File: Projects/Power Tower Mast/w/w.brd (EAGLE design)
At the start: 15 x 20.9 mm, 25 parts

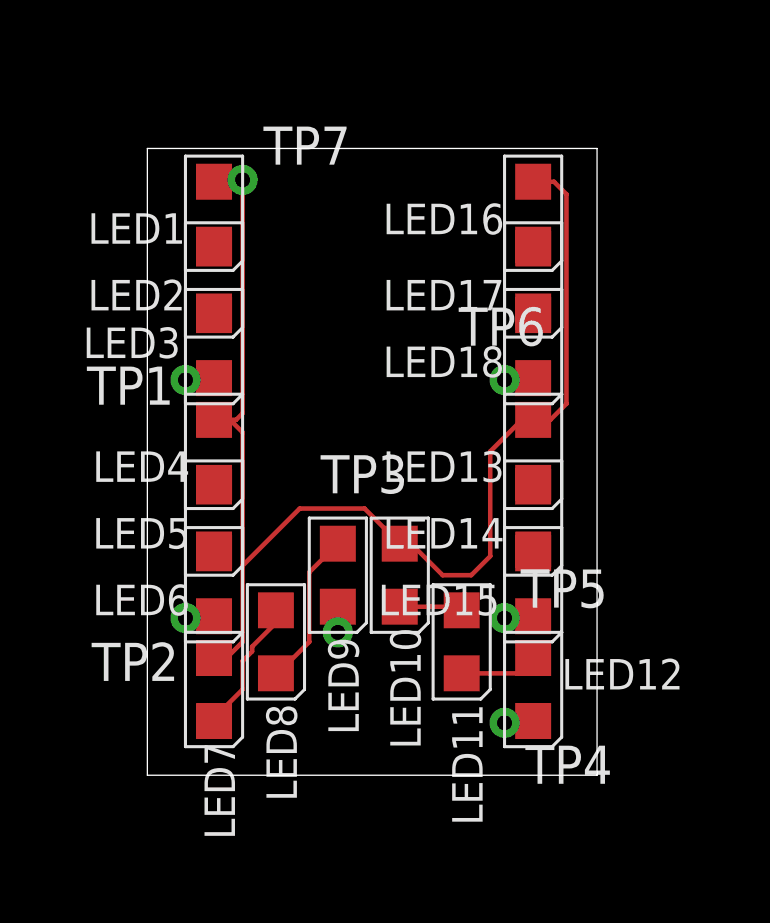
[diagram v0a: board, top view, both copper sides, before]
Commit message: updated with extra vias and panelized
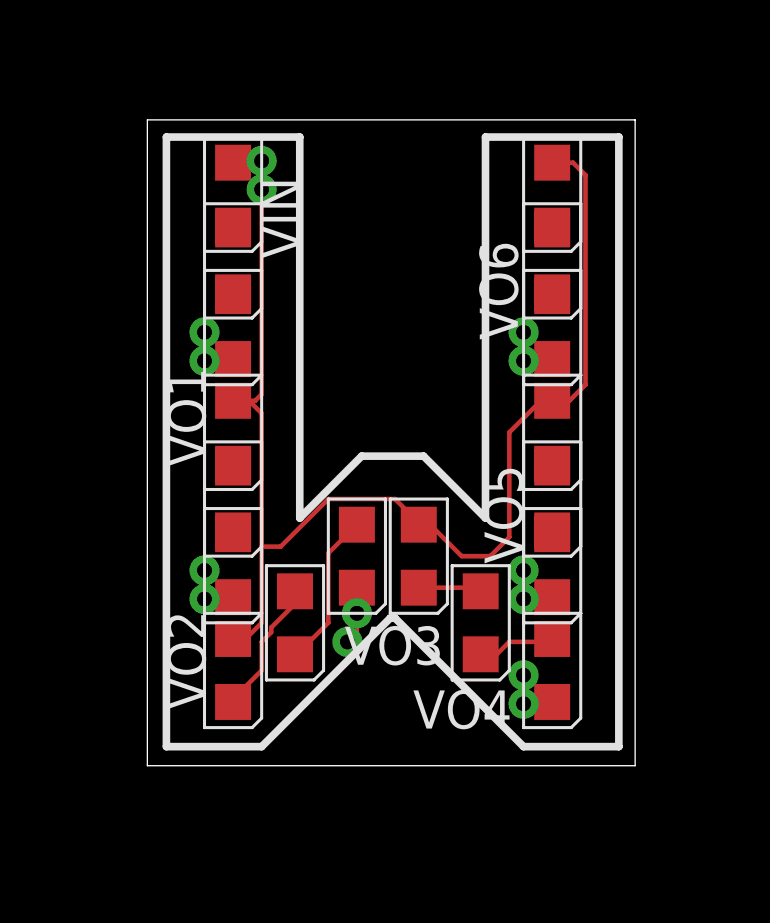
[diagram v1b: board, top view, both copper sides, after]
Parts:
- removed TP1, TP2, TP3, TP4, TP5, TP6, TP7: (no value), CyberRailGuru:P1-20
- added VIN, VIN1, VO1, VO10, VO11, VO12, VO2, VO3, VO4, VO5, VO6, VO7, VO8, VO9: (no value), CyberRailGuru:P1-20
- moved LED1 0.90 mm to (2.86, 19.1)
- moved LED11 0.90 mm to (11.1, 4.76)
- moved LED13 0.90 mm to (13.5, 11.1)
- moved LED16 0.90 mm to (13.5, 19.1)
- moved LED17 0.90 mm to (13.5, 16.8)
- moved LED2 0.90 mm to (2.86, 16.8)
- moved LED4 0.90 mm to (2.86, 11.1)
- moved LED9 0.90 mm to (6.99, 6.99)
- moved LED10 0.90 mm to (9.05, 6.99)
- moved LED15 0.90 mm to (13.5, 6.67)
- moved LED6 0.90 mm to (2.86, 6.67)
- moved LED12 0.90 mm to (13.5, 3.17)
- moved LED14 0.90 mm to (13.5, 8.89)
- moved LED18 0.90 mm to (13.5, 14.6)
- moved LED3 0.90 mm to (2.86, 14.6)
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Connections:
- removed net VIN3: LED1.A, LED10.A, LED13.A, LED16.A, LED4.A, LED7.A, TP7.TP
- removed net VOUT14: LED3.C, TP1.TP
- removed net VOUT15: LED6.C, TP2.TP
- removed net VOUT16: LED9.C, TP3.TP
- removed net VOUT17: LED12.C, TP4.TP
- removed net VOUT18: LED15.C, TP5.TP
- removed net VOUT19: LED18.C, TP6.TP
- new net VIN: LED1.A, LED10.A, LED13.A, LED16.A, LED4.A, LED7.A, VIN.TP, VIN1.TP
- new net VOUT1: LED3.C, VO1.TP, VO7.TP
- new net VOUT2: LED6.C, VO2.TP, VO8.TP
- new net VOUT3: LED9.C, VO3.TP, VO9.TP
- new net VOUT4: LED12.C, VO10.TP, VO4.TP
- new net VOUT5: LED15.C, VO11.TP, VO5.TP
- new net VOUT6: LED18.C, VO12.TP, VO6.TP
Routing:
- net VIN3: track 44.3 -> 0.00 mm
- net VIN: track 0.00 -> 44.0 mm
- net VOUT3: track 0.00 -> 1.94 mm
- net VOUT4: track 0.00 -> 1.93 mm
- net VOUT5: track 0.00 -> 1.93 mm
- net VOUT2: track 0.00 -> 1.93 mm
- net VOUT6: track 0.00 -> 1.93 mm
- net VOUT1: track 0.00 -> 1.93 mm
- net VOUT18: track 0.98 -> 0.00 mm
- net VOUT17: track 0.98 -> 0.00 mm
- net VOUT15: track 0.98 -> 0.00 mm
- net VOUT19: track 0.98 -> 0.00 mm
- net VOUT14: track 0.98 -> 0.00 mm
- net VOUT16: track 0.85 -> 0.00 mm
- net N$33: track 2.59 -> 3.32 mm
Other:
- board size 15 x 20.9 mm -> 16.3 x 21.5 mm

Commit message: reworking some letters
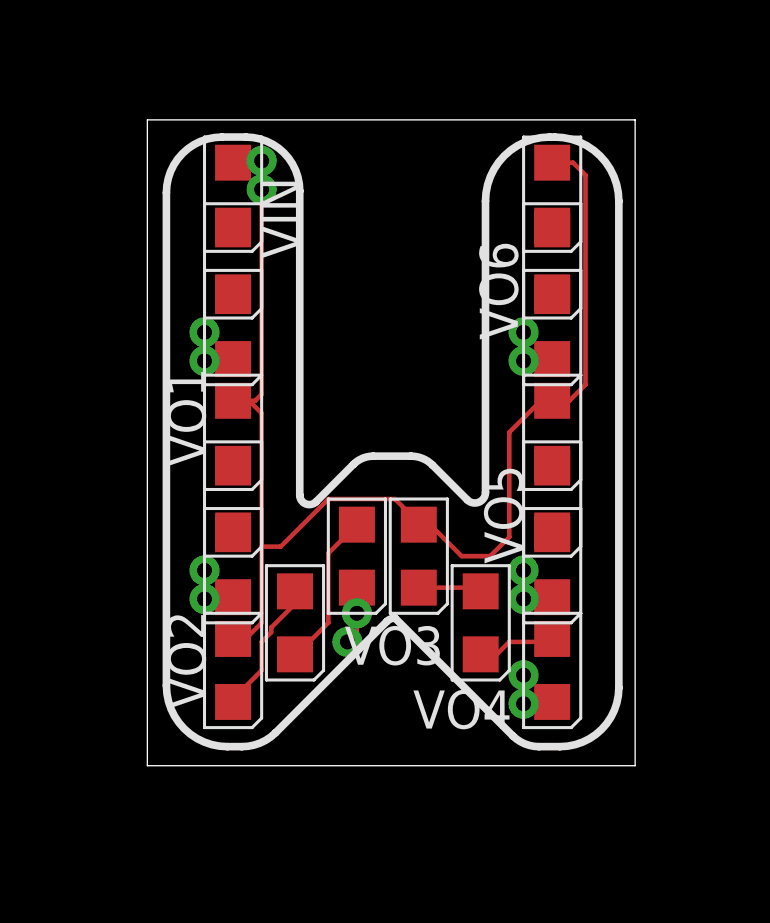
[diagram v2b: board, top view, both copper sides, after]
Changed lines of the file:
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@@
 <wire x1="0" y1="21.52736875" x2="0" y2="0" width="0" layer="20"/>
 <text x="0.635" y="0.635" size="20.32" layer="201" font="fixed" ratio="22" distance="27">W</text>
-<wire x1="0.635" y1="20.955" x2="5.08" y2="20.955" width="0.254" layer="21"/>
-<wire x1="5.08" y1="20.955" x2="5.08" y2="8.255" width="0.254" layer="21"/>
-<wire x1="0.635" y1="20.955" x2="0.635" y2="0.635" width="0.254" layer="21"/>
-<wire x1="0.635" y1="0.635" x2="3.81" y2="0.635" width="0.254" layer="21"/>
-<wire x1="12.54125" y1="0.635" x2="15.71625" y2="0.635" width="0.254" layer="21"/>
-<wire x1="15.71625" y1="0.635" x2="15.71625" y2="20.955" width="0.254" layer="21"/>
-<wire x1="15.71625" y1="20.955" x2="11.27125" y2="20.955" width="0.254" layer="21"/>
-<wire x1="11.27125" y1="20.955" x2="11.27125" y2="8.255" width="0.254" layer="21"/>
-<wire x1="11.27125" y1="8.255" x2="9.2075" y2="10.31875" width="0.254" layer="21"/>
-<wire x1="9.2075" y1="10.31875" x2="7.14375" y2="10.31875" width="0.254" layer="21"/>
-<wire x1="7.14375" y1="10.31875" x2="5.08" y2="8.255" width="0.254" layer="21"/>
-<wire x1="3.81" y1="0.635" x2="8.09625" y2="4.92125" width="0.254" layer="21"/>
-<wire x1="8.09625" y1="4.92125" x2="8.255" y2="4.92125" width="0.254" layer="21"/>
-<wire x1="8.255" y1="4.92125" x2="12.54125" y2="0.635" width="0.254" layer="21"/>
+<wire x1="2.486325" y1="20.955" x2="3.28395" y2="20.955" width="0.254" layer="21"/>
+<wire x1="3.28395" y1="20.955" x2="5.08" y2="19.15895" width="0.254" layer="21" curve="-90"/>
+<wire x1="6.87263125" y1="10.04763125" x2="5.62200625" y2="8.79700625" width="0.254" layer="21"/>
+<wire x1="5.62200625" y1="8.79700625" x2="5.08" y2="9.0215125" width="0.254" layer="21" curve="-135"/>
+<wire x1="5.08" y1="9.0215125" x2="5.08" y2="19.15895" width="0.254" layer="21"/>
+<wire x1="2.486325" y1="20.955" x2="0.635" y2="19.103675" width="0.254" layer="21" curve="90"/>
+<wire x1="0.635" y1="19.103675" x2="0.635" y2="2.667990625" width="0.254" layer="21"/>
+<wire x1="0.635" y1="2.667990625" x2="2.667990625" y2="0.635" width="0.254" layer="21" curve="90"/>
+<wire x1="2.667990625" y1="0.635" x2="3.1524375" y2="0.635" width="0.254" layer="21"/>
+<wire x1="3.1524375" y1="0.635" x2="4.27496875" y2="1.09996875" width="0.254" layer="21" curve="45"/>
+<wire x1="4.27496875" y1="1.09996875" x2="7.983996875" y2="4.808996875" width="0.254" layer="21"/>
+<wire x1="8.255" y1="4.92125" x2="12.1781" y2="0.99815" width="0.254" layer="21"/>
+<wire x1="12.1781" y1="0.99815" x2="13.054821875" y2="0.635" width="0.254" layer="21" curve="44.999856"/>
+<wire x1="13.054821875" y1="0.635" x2="13.752621875" y2="0.635" width="0.254" layer="21"/>
+<wire x1="13.752621875" y1="0.635" x2="15.71625" y2="2.598628125" width="0.254" layer="21" curve="90"/>
+<wire x1="15.71625" y1="2.598628125" x2="15.71625" y2="18.8192375" width="0.254" layer="21"/>
+<wire x1="15.71625" y1="18.8192375" x2="13.5804875" y2="20.955" width="0.254" layer="21" curve="90"/>
+<wire x1="13.5804875" y1="20.955" x2="13.4070125" y2="20.955" width="0.254" layer="21"/>
+<wire x1="13.4070125" y1="20.955" x2="11.27125" y2="18.8192375" width="0.254" layer="21" curve="90"/>
+<wire x1="11.27125" y1="18.8192375" x2="11.27125" y2="9.111984375" width="0.254" layer="21"/>
+<wire x1="11.27125" y1="9.111984375" x2="10.66526875" y2="8.86098125" width="0.254" layer="21" curve="-135.000357"/>
+<wire x1="10.66526875" y1="8.86098125" x2="9.505225" y2="10.021025" width="0.254" layer="21"/>
+<wire x1="9.505225" y1="10.021025" x2="8.786453125" y2="10.31875" width="0.254" layer="21" curve="45.000176"/>
+<wire x1="8.786453125" y1="10.31875" x2="7.527171875" y2="10.31875" width="0.254" layer="21"/>
+<wire x1="7.527171875" y1="10.31875" x2="6.87263125" y2="10.04763125" width="0.254" layer="21" curve="44.999863"/>
+<wire x1="7.983996875" y1="4.808996875" x2="8.255" y2="4.92125" width="0.254" layer="21" curve="-45"/>
 </plain>
 <attributes>

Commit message: fixed ratio for all letters; continued to update layouts
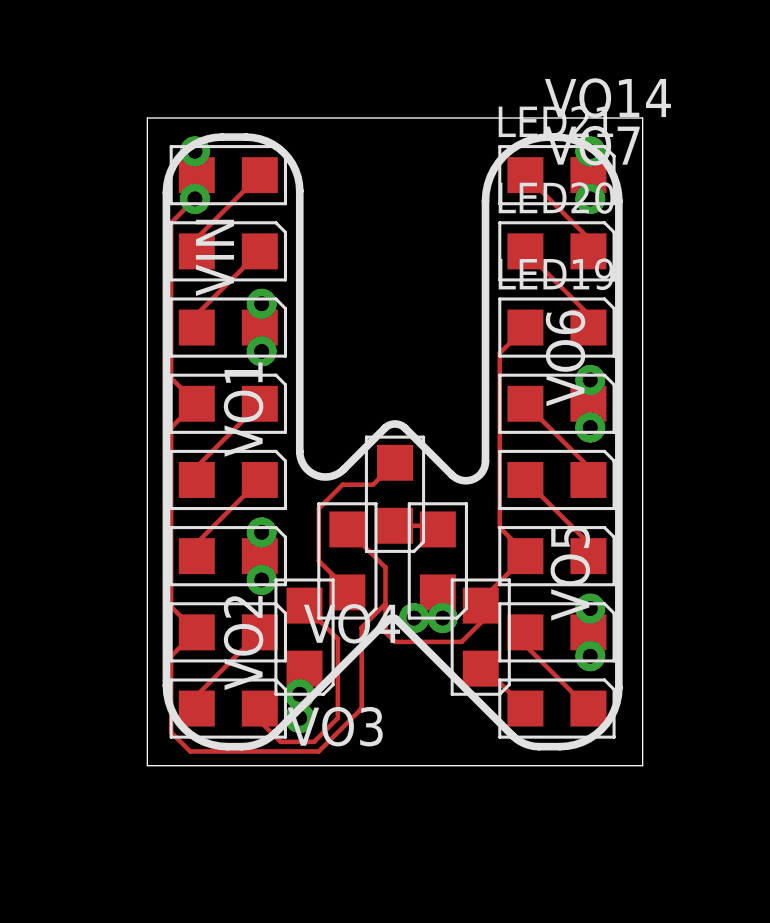
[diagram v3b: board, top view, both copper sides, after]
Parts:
- added LED19, LED20, LED21: (no value), CyberRailGuru:LED_0805
- added VO13, VO14: (no value), CyberRailGuru:P1-20
- moved VO7 13.6 mm to (14.8, 18.9)
- moved LED16 12.1 mm to (13.7, 6.99), turned to 270 degrees
- moved VO12 9.47 mm to (14.8, 5.24)
- moved VO8 9.09 mm to (3.81, 15.4)
- moved VO10 7.60 mm to (5.08, 1.59)
- moved LED17 7.30 mm to (13.7, 9.53), turned to 270 degrees
- moved LED13 7.23 mm to (11.1, 4.29)
- moved LED14 6.99 mm to (13.7, 1.91), turned to 270 degrees
- moved LED12 5.28 mm to (9.68, 6.83)
- moved LED11 5.15 mm to (8.26, 9.05)
- moved VO4 4.64 mm to (8.89, 4.92)
- moved VO9 4.64 mm to (3.81, 7.78)
- moved LED8 3.62 mm to (2.70, 1.91), turned to 270 degrees
- moved VO3 3.30 mm to (5.08, 2.38)
- moved LED9 3.21 mm to (5.24, 4.29)
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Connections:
- new net N$1: LED19.C, LED20.A
- new net N$2: LED20.C, LED21.A
- new net VOUT7: LED21.C, VO14.TP, VO7.TP
- net VIN: now also LED19.A
- net VOUT1: now also VO8.TP; no longer VO7.TP
- net VOUT2: now also VO9.TP; no longer VO8.TP
- net VOUT3: now also VO10.TP; no longer VO9.TP
- net VOUT4: now also VO11.TP; no longer VO10.TP
- net VOUT5: now also VO12.TP; no longer VO11.TP
- net VOUT6: now also VO13.TP; no longer VO12.TP
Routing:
- net VIN: track 44.0 -> 51.0 mm
- net N$34: track 2.11 -> 6.36 mm
- net N$2: track 0.00 -> 3.41 mm
- net N$1: track 0.00 -> 3.41 mm
- net N$38: track 0.12 -> 3.41 mm
- net N$35: track 0.12 -> 3.41 mm
- net N$26: track 0.12 -> 3.41 mm
- net N$37: track 0.12 -> 3.41 mm
- net N$29: track 0.12 -> 3.41 mm
- net N$30: track 0.12 -> 3.41 mm
- net N$25: track 0.12 -> 3.41 mm
- net N$31: track 5.21 -> 7.84 mm
- net N$36: track 0.12 -> 2.04 mm
- net N$33: track 3.32 -> 1.48 mm
- net VOUT7: track 0.00 -> 1.64 mm
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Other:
- board size 16.3 x 21.5 mm -> 16.5 x 21.6 mm

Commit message: final updates before fab.  added new letters for future projects.
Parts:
- moved VO10 1.99 mm to (6.03, 3.33)
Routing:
- net VIN: track 51.0 -> 42.1 mm, vias 0 -> 3
- net N$31: track 7.84 -> 4.17 mm, vias 0 -> 2
- net N$34: track 6.36 -> 4.98 mm, vias 0 -> 2
